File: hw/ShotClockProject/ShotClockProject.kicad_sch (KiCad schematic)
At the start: 5 parts, among them SW5 SW_SPST

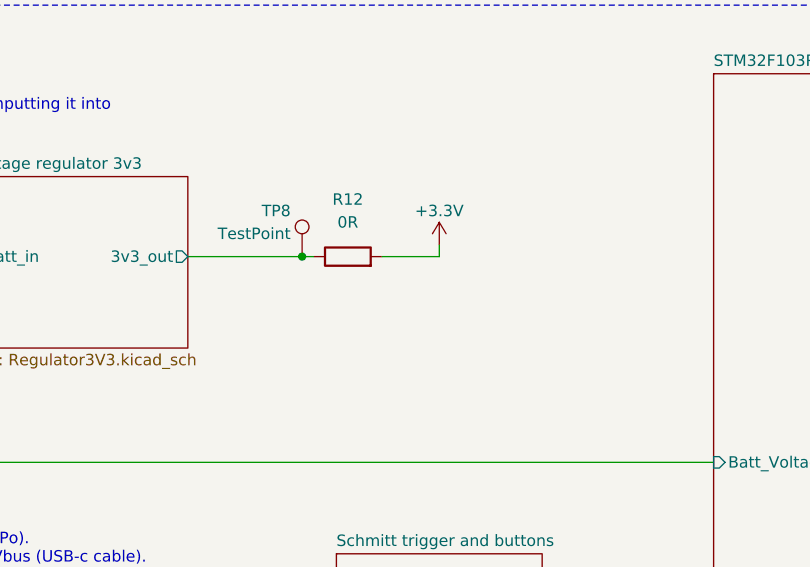
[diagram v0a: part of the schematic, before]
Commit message: Fixed all ERC issues
Mainly by placing PWR_FLAGs and NetTies to show KiCAD where the GNDs are connected to each other physically, without them being the same net.
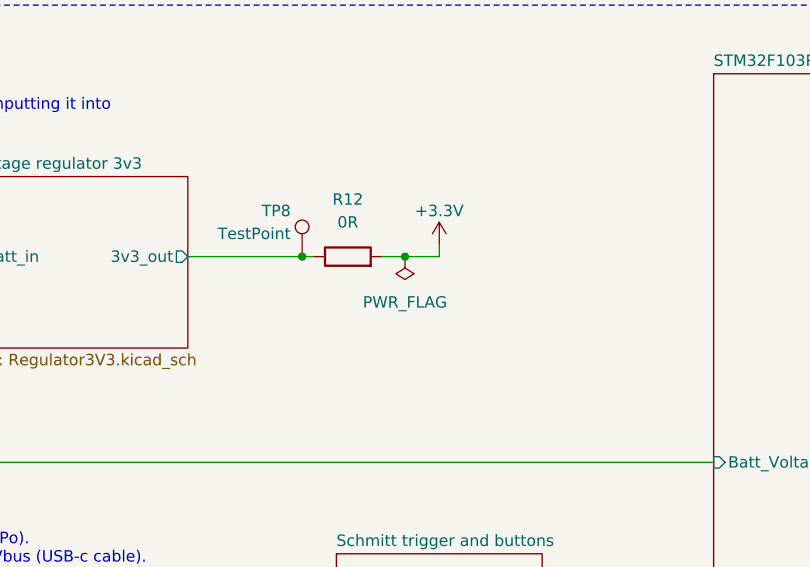
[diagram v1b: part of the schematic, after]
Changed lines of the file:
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@@
     (date "2023-06-28")
     (rev "1")
+    (comment 1 "Author: M. de Waard")
   )
   (junction (at 59.69 49.53) (diameter 0) (color 0 0 0 0)
   )
+  (junction (at 130.81 49.53) (diameter 0) (color 0 0 0 0)
+  )
   (junction (at 119.38 49.53) (diameter 0) (color 0 0 0 0)
   )
@@
     (stroke (width 0) (type default))
   )
-  (wire (pts (xy 128.27 49.53) (xy 134.62 49.53))
+  (wire (pts (xy 128.27 49.53) (xy 130.81 49.53))
     (stroke (width 0) (type default))
   )
@@
   )
   (wire (pts (xy 203.2 78.74) (xy 231.14 78.74))
+    (stroke (width 0) (type default))
+  )
+  (wire (pts (xy 130.81 49.53) (xy 134.62 49.53))
     (stroke (width 0) (type default))
   )
@@
         )
       )
+    )
+  )
+  (symbol (lib_id "power:PWR_FLAG") (at 130.81 49.53 180) (unit 1)
+    (in_bom yes) (on_board yes) (dnp no) (fields_autoplaced)
+    (property "Reference" "#FLG02" (at 130.81 51.435 0)
+      (effects (font (size 1.27 1.27)) hide)
+    )
+    (property "Value" "PWR_FLAG" (at 130.81 54.61 0)
+      (effects (font (size 1.27 1.27)))
+    )
+    (property "Footprint" "" (at 130.81 49.53 0)
+      (effects (font (size 1.27 1.27)) hide)
+    )
+    (property "Datasheet" "~" (at 130.81 49.53 0)
+      (effects (font (size 1.27 1.27)) hide)
+    )
+    (pin "1")
+    (instances
+      (project "ShotClockProject"
+        (path "/5fd859aa-754d-49c2-9762-3f7ebe3bb64c/d53b1cd8-24cb-4dc0-9a02-0cd96c1f4291"
+          (reference "#FLG02") (unit 1)
+        )
+        (path "/5fd859aa-754d-49c2-9762-3f7ebe3bb64c/d287d155-1951-4d4f-8d6c-570f03bc79f5"
+          (reference "#FLG04") (unit 1)
+        )
+        (path "/5fd859aa-754d-49c2-9762-3f7ebe3bb64c"
+          (reference "#FLG03") (unit 1)
+        )
+      )

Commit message: Finished footprint selection & updated design doc
Chosen all footprints
Updated design doc with part link & part selection reasons
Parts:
- R12, R8: footprint (none) -> Resistor_SMD:R_0603_1608Metric
- SW5: footprint (none) -> Button_Switch_SMD:SW_SPDT_PCM12
- TP1, TP8: footprint (none) -> TestPoint:TestPoint_Pad_D2.5mm
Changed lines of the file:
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@@
       (effects (font (size 1.27 1.27)))
     )
-    (property "Footprint" "" (at 76.2 49.53 0)
+    (property "Footprint" "Button_Switch_SMD:SW_SPDT_PCM12" (at 76.2 49.53 0)
       (effects (font (size 1.27 1.27)) hide)
     )
@@
       (effects (font (size 1.27 1.27)))
     )
-    (property "Footprint" "" (at 64.77 51.308 90)
+    (property "Footprint" "Resistor_SMD:R_0603_1608Metric" (at 64.77 51.308 90)
       (effects (font (size 1.27 1.27)) hide)
     )
@@
       (effects (font (size 1.27 1.27)) (justify left))
     )
-    (property "Footprint" "" (at 114.3 49.53 0)
+    (property "Footprint" "TestPoint:TestPoint_Pad_D2.5mm" (at 114.3 49.53 0)
       (effects (font (size 1.27 1.27)) hide)
     )
@@
       (effects (font (size 1.27 1.27)))
     )
-    (property "Footprint" "" (at 124.46 51.308 90)
+    (property "Footprint" "Resistor_SMD:R_0603_1608Metric" (at 124.46 51.308 90)
       (effects (font (size 1.27 1.27)) hide)
     )
@@
       (effects (font (size 1.27 1.27)) (justify left))
     )
-    (property "Footprint" "" (at 54.61 49.53 0)
+    (property "Footprint" "TestPoint:TestPoint_Pad_D2.5mm" (at 54.61 49.53 0)
       (effects (font (size 1.27 1.27)) hide)
     )

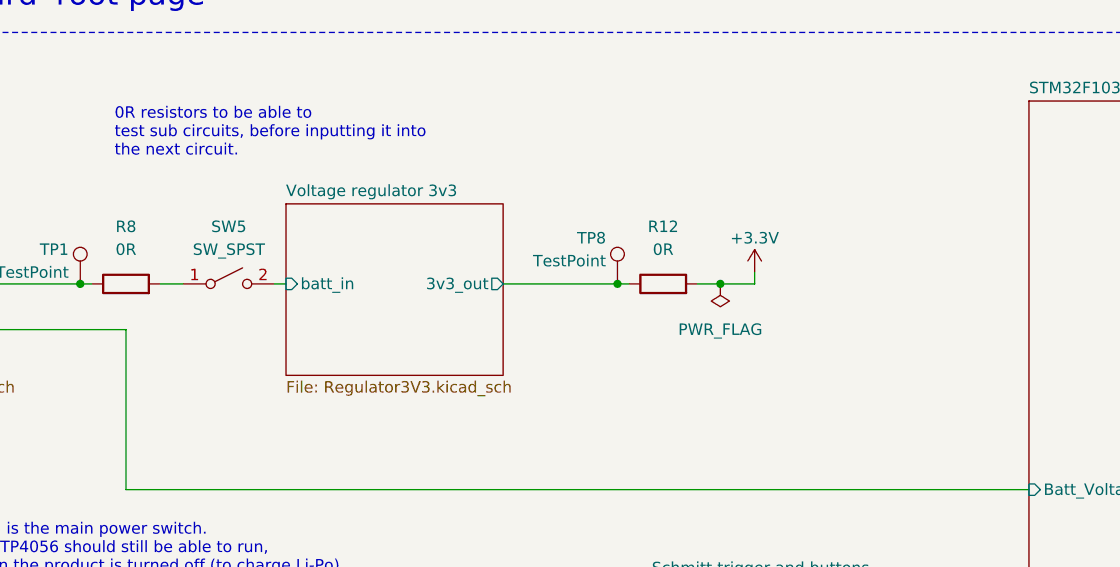
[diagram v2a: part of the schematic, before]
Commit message: HW changes
Changed Switches to correct SPDT instead of SPST.
Added design requirements to PCB according to JLCPCB specs
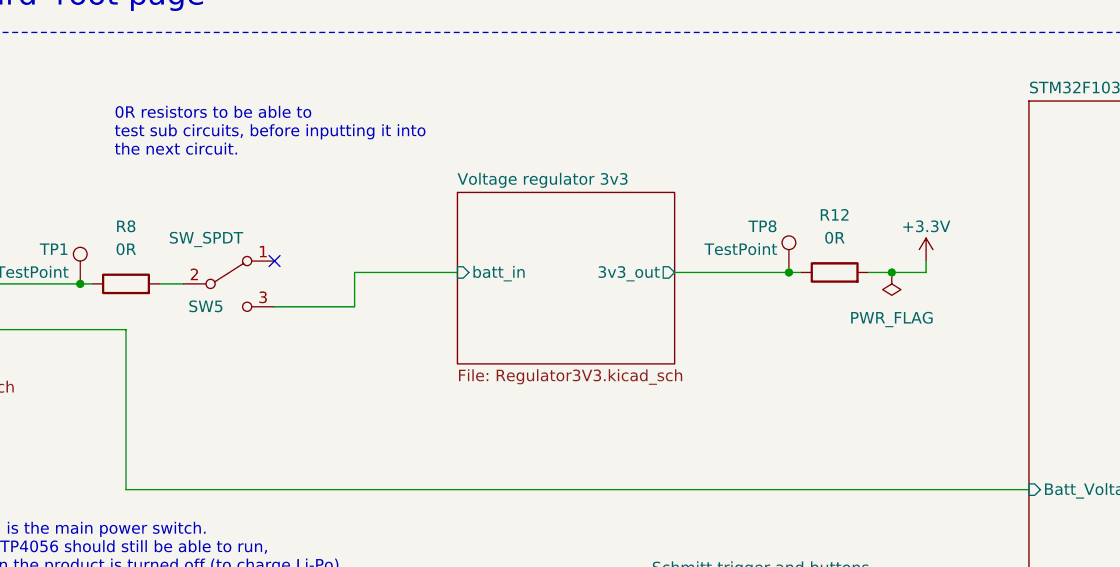
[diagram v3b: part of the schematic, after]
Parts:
- removed SW5: SW_SPST, Button_Switch_SMD:SW_SPDT_PCM12, symbol Switch:SW_SPST
- added SW5: SW_SPDT, Button_Switch_SMD:SW_SPDT_PCM12, symbol Switch:SW_SPDT
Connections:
- net Voltage regulator 3v3/batt_in: now also SW5.3 (C)
- net at R8.2: now also SW5.2 (B)
- no-connect marks 0 -> 1
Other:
- moved on the sheet: R12, TP8
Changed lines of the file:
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@@
   (junction (at 59.69 49.53) (diameter 0) (color 0 0 0 0)
   )
-  (junction (at 130.81 49.53) (diameter 0) (color 0 0 0 0)
-  )
-  (junction (at 119.38 49.53) (diameter 0) (color 0 0 0 0)
-  )
+  (junction (at 149.86 48.26) (diameter 0) (color 0 0 0 0)
+  )
+  (junction (at 138.43 48.26) (diameter 0) (color 0 0 0 0)
+  )
+  (no_connect (at 81.28 46.99))
   (wire (pts (xy 203.2 50.8) (xy 231.14 50.8))
     (stroke (width 0) (type default))
@@
     (stroke (width 0) (type default))
   )
-  (wire (pts (xy 119.38 49.53) (xy 120.65 49.53))
+  (wire (pts (xy 138.43 48.26) (xy 139.7 48.26))
     (stroke (width 0) (type default))
   )
@@
     (stroke (width 0) (type default))
   )
-  (wire (pts (xy 81.28 49.53) (xy 82.55 49.53))
+  (wire (pts (xy 90.17 48.26) (xy 101.6 48.26))
     (stroke (width 0) (type default))
   )
@@
     (stroke (width 0) (type default))
   )
-  (wire (pts (xy 106.68 49.53) (xy 119.38 49.53))
+  (wire (pts (xy 125.73 48.26) (xy 138.43 48.26))
     (stroke (width 0) (type default))
   )
@@
     (stroke (width 0) (type default))
   )
-  (wire (pts (xy 134.62 49.53) (xy 134.62 48.26))
+  (wire (pts (xy 153.67 48.26) (xy 153.67 46.99))
     (stroke (width 0) (type default))
   )
@@
     (stroke (width 0) (type default))
   )
-  (wire (pts (xy 128.27 49.53) (xy 130.81 49.53))
+  (wire (pts (xy 147.32 48.26) (xy 149.86 48.26))
     (stroke (width 0) (type default))
   )
@@
     (stroke (width 0) (type default))
   )
+  (wire (pts (xy 90.17 52.07) (xy 90.17 48.26))
+    (stroke (width 0) (type default))
+  )
   (wire (pts (xy 203.2 78.74) (xy 231.14 78.74))
     (stroke (width 0) (type default))
   )
-  (wire (pts (xy 130.81 49.53) (xy 134.62 49.53))
+  (wire (pts (xy 149.86 48.26) (xy 153.67 48.26))
     (stroke (width 0) (type default))
   )
   (wire (pts (xy 203.2 90.17) (xy 231.14 90.17))
+    (stroke (width 0) (type default))
+  )
+  (wire (pts (xy 81.28 52.07) (xy 90.17 52.07))
     (stroke (width 0) (type default))
   )
@@
     (effects (font (size 1.27 1.27)) (justify left bottom))
   )
-  (symbol (lib_id "Switch:SW_SPST") (at 76.2 49.53 0) (unit 1)
-    (in_bom yes) (on_board yes) (dnp no) (fields_autoplaced)
-    (property "Reference" "SW5" (at 76.2 43.18 0)
-      (effects (font (size 1.27 1.27)))
-    )
-    (property "Value" "SW_SPST" (at 76.2 45.72 0)
+  (symbol (lib_id "Switch:SW_SPDT") (at 76.2 49.53 0) (unit 1)
+    (in_bom yes) (on_board yes) (dnp no)
+    (property "Reference" "SW5" (at 73.66 52.07 0)
+      (effects (font (size 1.27 1.27)))
+    )
+    (property "Value" "SW_SPDT" (at 73.66 44.45 0)
       (effects (font (size 1.27 1.27)))
     )
@@
     (pin "1")
     (pin "2")
+    (pin "3")
     (instances
       (project "ShotClockProject"
         (path "/5fd859aa-754d-49c2-9762-3f7ebe3bb64c"
           (reference "SW5") (unit 1)
+        )
+        (path "/5fd859aa-754d-49c2-9762-3f7ebe3bb64c/d53b1cd8-24cb-4dc0-9a02-0cd96c1f4291"
+          (reference "SW1") (unit 1)
         )
       )
@@
     )
   )
-  (symbol (lib_id "Connector:TestPoint") (at 119.38 49.53 0) (mirror y) (unit 1)
+  (symbol (lib_id "Connector:TestPoint") (at 138.43 48.26 0) (mirror y) (unit 1)
     (in_bom yes) (on_board yes) (dnp no)
-    (property "Reference" "TP8" (at 118.11 44.45 0)
-      (effects (font (size 1.27 1.27)) (justify left))
-    )
-    (property "Value" "TestPoint" (at 118.11 46.99 0)
-      (effects (font (size 1.27 1.27)) (justify left))
-    )
-    (property "Footprint" "TestPoint:TestPoint_Pad_D2.5mm" (at 114.3 49.53 0)
-      (effects (font (size 1.27 1.27)) hide)
-    )
-    (property "Datasheet" "~" (at 114.3 49.53 0)
+    (property "Reference" "TP8" (at 137.16 43.18 0)
+      (effects (font (size 1.27 1.27)) (justify left))
+    )
+    (property "Value" "TestPoint" (at 137.16 45.72 0)
+      (effects (font (size 1.27 1.27)) (justify left))
+    )
+    (property "Footprint" "TestPoint:TestPoint_Pad_D2.5mm" (at 133.35 48.26 0)
+      (effects (font (size 1.27 1.27)) hide)
+    )
+    (property "Datasheet" "~" (at 133.35 48.26 0)
       (effects (font (size 1.27 1.27)) hide)
     )
@@
     )
   )
-  (symbol (lib_id "Device:R") (at 124.46 49.53 90) (unit 1)
+  (symbol (lib_id "Device:R") (at 143.51 48.26 90) (unit 1)
     (in_bom yes) (on_board yes) (dnp no) (fields_autoplaced)
-    (property "Reference" "R12" (at 124.46 43.18 90)
-      (effects (font (size 1.27 1.27)))
-    )
-    (property "Value" "0R" (at 124.46 45.72 90)
-      (effects (font (size 1.27 1.27)))
-    )
-    (property "Footprint" "Resistor_SMD:R_0603_1608Metric" (at 124.46 51.308 90)
-      (effects (font (size 1.27 1.27)) hide)
-    )
-    (property "Datasheet" "~" (at 124.46 49.53 0)
+    (property "Reference" "R12" (at 143.51 41.91 90)
+      (effects (font (size 1.27 1.27)))
+    )
+    (property "Value" "0R" (at 143.51 44.45 90)
+      (effects (font (size 1.27 1.27)))
+    )
+    (property "Footprint" "Resistor_SMD:R_0603_1608Metric" (at 143.51 50.038 90)
+      (effects (font (size 1.27 1.27)) hide)
+    )
+    (property "Datasheet" "~" (at 143.51 48.26 0)
       (effects (font (size 1.27 1.27)) hide)
     )
@@
     )
   )
-  (symbol (lib_id "power:PWR_FLAG") (at 130.81 49.53 180) (unit 1)
+  (symbol (lib_id "power:PWR_FLAG") (at 149.86 48.26 180) (unit 1)
     (in_bom yes) (on_board yes) (dnp no) (fields_autoplaced)
-    (property "Reference" "#FLG02" (at 130.81 51.435 0)
-      (effects (font (size 1.27 1.27)) hide)
-    )
-    (property "Value" "PWR_FLAG" (at 130.81 54.61 0)
-      (effects (font (size 1.27 1.27)))
-    )
-    (property "Footprint" "" (at 130.81 49.53 0)
-      (effects (font (size 1.27 1.27)) hide)
-    )
-    (property "Datasheet" "~" (at 130.81 49.53 0)
+    (property "Reference" "#FLG02" (at 149.86 50.165 0)
+      (effects (font (size 1.27 1.27)) hide)
+    )
+    (property "Value" "PWR_FLAG" (at 149.86 53.34 0)
+      (effects (font (size 1.27 1.27)))
+    )
+    (property "Footprint" "" (at 149.86 48.26 0)
+      (effects (font (size 1.27 1.27)) hide)
+    )
+    (property "Datasheet" "~" (at 149.86 48.26 0)
       (effects (font (size 1.27 1.27)) hide)
     )
@@
     )
   )
-  (symbol (lib_id "power:+3.3V") (at 134.62 48.26 0) (unit 1)
+  (symbol (lib_id "power:+3.3V") (at 153.67 46.99 0) (unit 1)
     (in_bom yes) (on_board yes) (dnp no)
-    (property "Reference" "#PWR033" (at 134.62 52.07 0)
-      (effects (font (size 1.27 1.27)) hide)
-    )
-    (property "Value" "+3.3V" (at 134.62 44.45 0)
-      (effects (font (size 1.27 1.27)))
-    )
-    (property "Footprint" "" (at 134.62 48.26 0)
-      (effects (font (size 1.27 1.27)) hide)
-    )
-    (property "Datasheet" "" (at 134.62 48.26 0)
+    (property "Reference" "#PWR033" (at 153.67 50.8 0)
+      (effects (font (size 1.27 1.27)) hide)
+    )
+    (property "Value" "+3.3V" (at 153.67 43.18 0)
+      (effects (font (size 1.27 1.27)))
+    )
+    (property "Footprint" "" (at 153.67 46.99 0)
+      (effects (font (size 1.27 1.27)) hide)
+    )
+    (property "Datasheet" "" (at 153.67 46.99 0)
       (effects (font (size 1.27 1.27)) hide)
     )
@@
     )
   )
-  (sheet (at 82.55 40.64) (size 24.13 19.05) (fields_autoplaced)
+  (sheet (at 101.6 39.37) (size 24.13 19.05) (fields_autoplaced)
     (stroke (width 0.1524) (type solid))
     (fill (color 0 0 0 0.0000))
-    (property "Sheetname" "Voltage regulator 3v3" (at 82.55 39.9284 0)
+    (property "Sheetname" "Voltage regulator 3v3" (at 101.6 38.6584 0)
       (effects (font (size 1.27 1.27)) (justify left bottom))
     )
-    (property "Sheetfile" "Regulator3V3.kicad_sch" (at 82.55 60.2746 0)
+    (property "Sheetfile" "Regulator3V3.kicad_sch" (at 101.6 59.0046 0)
       (effects (font (size 1.27 1.27)) (justify left top))
     )
-    (pin "batt_in" input (at 82.55 49.53 180)
-      (effects (font (size 1.27 1.27)) (justify left))
-    )
-    (pin "3v3_out" output (at 106.68 49.53 0)
+    (pin "batt_in" input (at 101.6 48.26 180)
+      (effects (font (size 1.27 1.27)) (justify left))
+    )
+    (pin "3v3_out" output (at 125.73 48.26 0)
       (effects (font (size 1.27 1.27)) (justify right))
     )
